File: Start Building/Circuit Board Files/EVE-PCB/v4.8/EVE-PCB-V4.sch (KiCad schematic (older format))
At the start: 50 parts, among them J1 PJ-102AH, J2 2x20 Male Header, J3 1725669, Q1 UA7805CKCT, Q12 DMN6140LQ-7, Q6 DMN6140LQ-7, Q7 DMN6140LQ-7, U1 PCA9685PW, U2 ADS1115IDGSR, U3 TLV4314IPWR, U4 TLV4314IPWR, U5 MCP1501-40E_SN

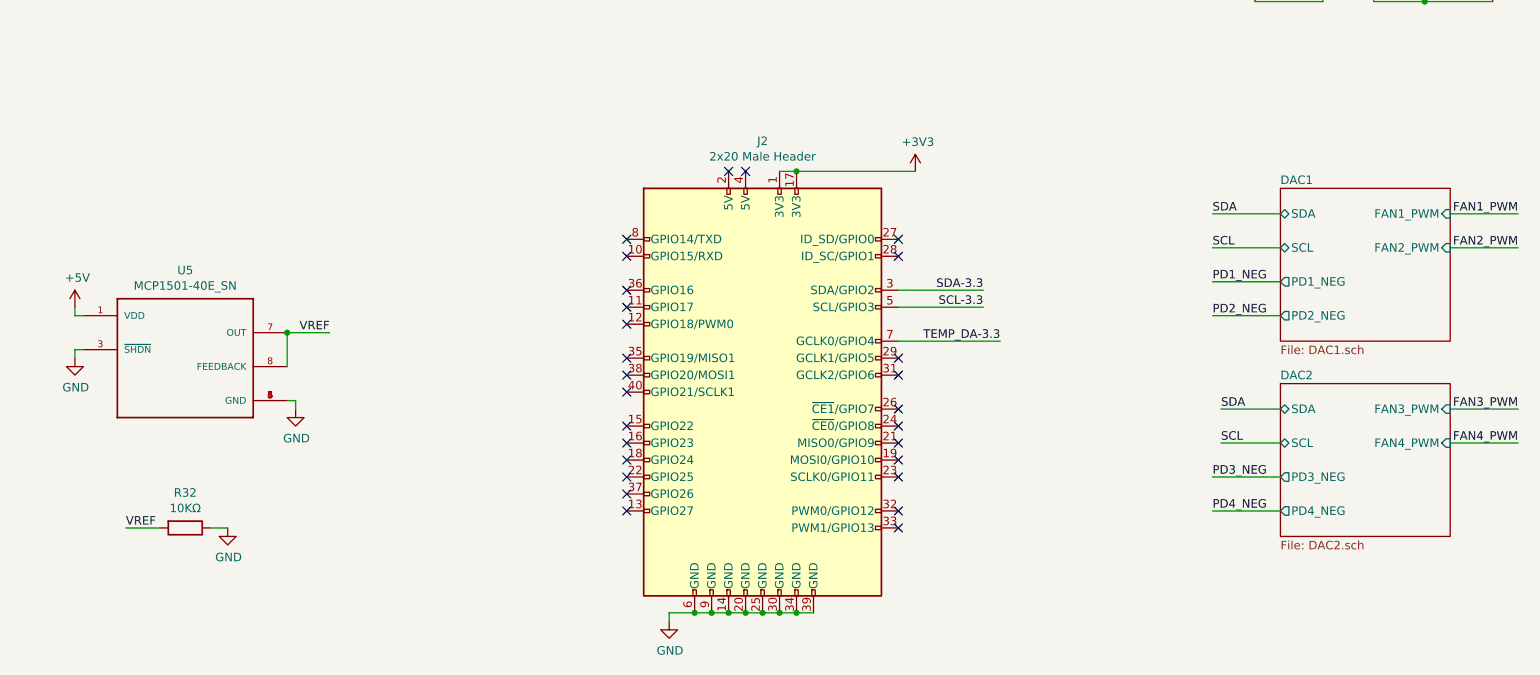
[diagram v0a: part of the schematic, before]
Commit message: Bump PCB version to 4.81
- Fixed voltages for fan and LED
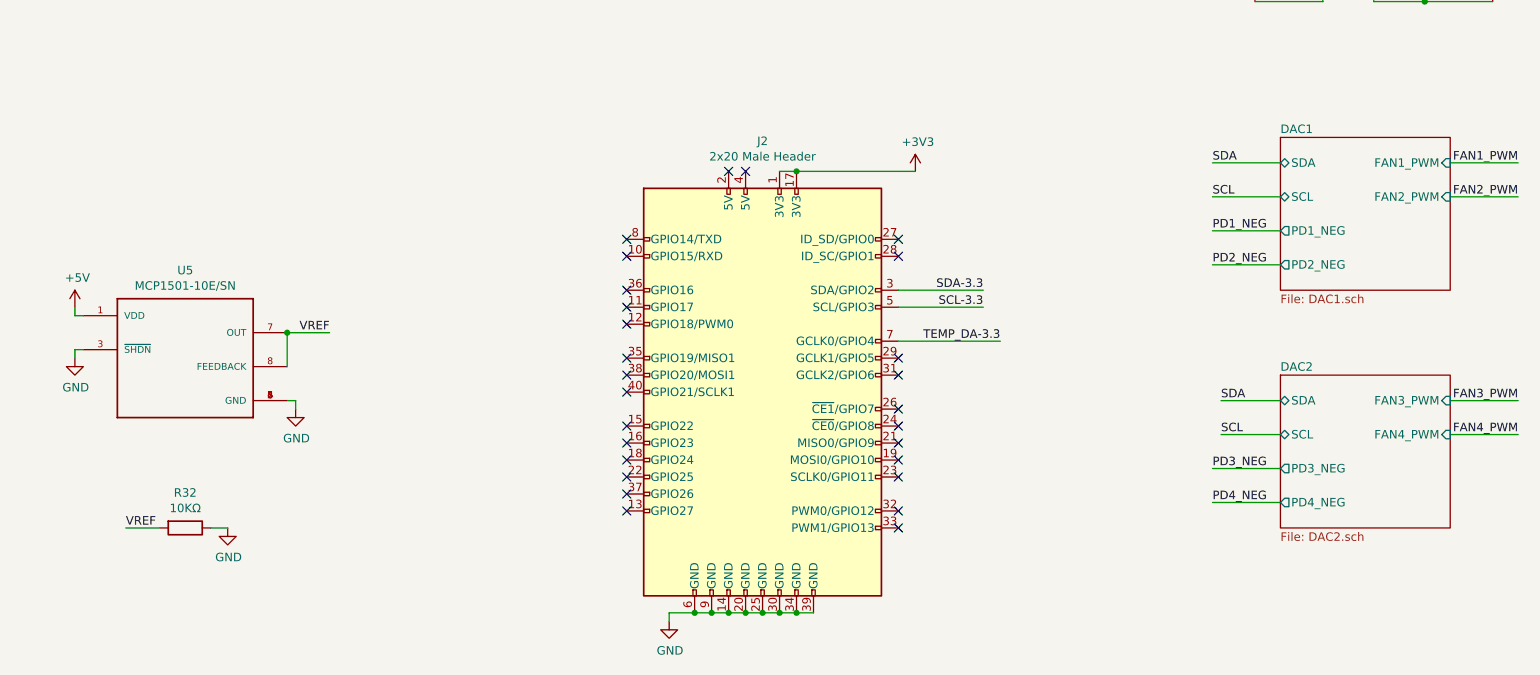
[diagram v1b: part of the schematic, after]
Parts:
- U5: value MCP1501-40E_SN -> MCP1501-10E/SN
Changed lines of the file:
@@
 P 7500 4600
 F 0 "U5" H 7500 5117 50  0000 C CNN
-F 1 "MCP1501-40E_SN" H 7500 5026 50  0000 C CNN
+F 1 "MCP1501-10E/SN" H 7500 5026 50  0000 C CNN
 F 2 "Package_SO:SOIC-8_3.9x4.9mm_P1.27mm" H 7500 4600 50  0001 L BNN
 F 3 "Microchip" H 7500 4600 50  0001 L BNN
@@
 $EndComp
 $Sheet
-S 13950 4750 1000 900
+S 13950 4700 1000 900
 U 5CA80A88
 F0 "DAC2" 50
 F1 "DAC2.sch" 50
-F2 "SDA" B L 13950 4900 50
-F3 "SCL" B L 13950 5100 50
-F4 "PD3_NEG" O L 13950 5300 50
-F5 "PD4_NEG" O L 13950 5500 50
-F6 "FAN3_PWM" I R 14950 4900 50
-F7 "FAN4_PWM" I R 14950 5100 50
+F2 "SDA" B L 13950 4850 50
+F3 "SCL" B L 13950 5050 50
+F4 "PD3_NEG" O L 13950 5250 50
+F5 "PD4_NEG" O L 13950 5450 50
+F6 "FAN3_PWM" I R 14950 4850 50
+F7 "FAN4_PWM" I R 14950 5050 50
 $EndSheet
 Wire Wire Line
-	15350 5100 14950 5100
-Wire Wire Line
-	15350 4900 14950 4900
-Text Label 15350 5100 2    50   ~ 0
+	15350 5050 14950 5050
+Wire Wire Line
+	15350 4850 14950 4850
+Text Label 15350 5050 2    50   ~ 0
 FAN4_PWM
-Text Label 15350 4900 2    50   ~ 0
+Text Label 15350 4850 2    50   ~ 0
 FAN3_PWM
 Wire Wire Line
-	15350 3950 14950 3950
-Wire Wire Line
-	15350 3750 14950 3750
-Text Label 15350 3950 2    50   ~ 0
+	15350 3650 14950 3650
+Wire Wire Line
+	15350 3450 14950 3450
+Text Label 15350 3650 2    50   ~ 0
 FAN2_PWM
-Text Label 15350 3750 2    50   ~ 0
+Text Label 15350 3450 2    50   ~ 0
 FAN1_PWM
 $Comp
@@
 $EndComp
 Wire Wire Line
-	13550 5500 13950 5500
-Wire Wire Line
-	13550 5300 13950 5300
-Text Label 13550 5500 0    50   ~ 0
+	13550 5450 13950 5450
+Wire Wire Line
+	13550 5250 13950 5250
+Text Label 13550 5450 0    50   ~ 0
 PD4_NEG
-Text Label 13550 5300 0    50   ~ 0
+Text Label 13550 5250 0    50   ~ 0
 PD3_NEG
 Wire Wire Line
-	13550 3950 13950 3950
-Wire Wire Line
-	13550 3750 13950 3750
-Text Label 13550 4150 0    50   ~ 0
+	13550 3650 13950 3650
+Wire Wire Line
+	13550 3450 13950 3450
+Text Label 13550 3850 0    50   ~ 0
 PD1_NEG
-Text Label 13550 4350 0    50   ~ 0
+Text Label 13550 4050 0    50   ~ 0
 PD2_NEG
 Wire Wire Line
-	13550 4150 13950 4150
-Wire Wire Line
-	13550 4350 13950 4350
+	13550 3850 13950 3850
+Wire Wire Line
+	13550 4050 13950 4050
 Connection ~ 14800 2100
 Wire Wire Line
@@
 	14800 1250 15300 1250
 Wire Wire Line
-	13600 5100 13950 5100
-Wire Wire Line
-	13600 4900 13950 4900
-Text Label 13600 5100 0    50   ~ 0
+	13600 5050 13950 5050
+Wire Wire Line
+	13600 4850 13950 4850
+Text Label 13600 5050 0    50   ~ 0
 SCL
-Text Label 13600 4900 0    50   ~ 0
+Text Label 13600 4850 0    50   ~ 0
 SDA
-Text Label 13550 3950 0    50   ~ 0
+Text Label 13550 3650 0    50   ~ 0
 SCL
-Text Label 13550 3750 0    50   ~ 0
+Text Label 13550 3450 0    50   ~ 0
 SDA
 $Sheet
-S 13950 3600 1000 900
+S 13950 3300 1000 900
 U 5CA7DFAE
 F0 "DAC1" 50
 F1 "DAC1.sch" 50
-F2 "SDA" B L 13950 3750 50
-F3 "SCL" B L 13950 3950 50
-F4 "PD1_NEG" O L 13950 4150 50
-F5 "PD2_NEG" O L 13950 4350 50
-F6 "FAN1_PWM" I R 14950 3750 50
-F7 "FAN2_PWM" I R 14950 3950 50
+F2 "SDA" B L 13950 3450 50
+F3 "SCL" B L 13950 3650 50
+F4 "PD1_NEG" O L 13950 3850 50
+F5 "PD2_NEG" O L 13950 4050 50
+F6 "FAN1_PWM" I R 14950 3450 50
+F7 "FAN2_PWM" I R 14950 3650 50
 $EndSheet
 Wire Wire Line

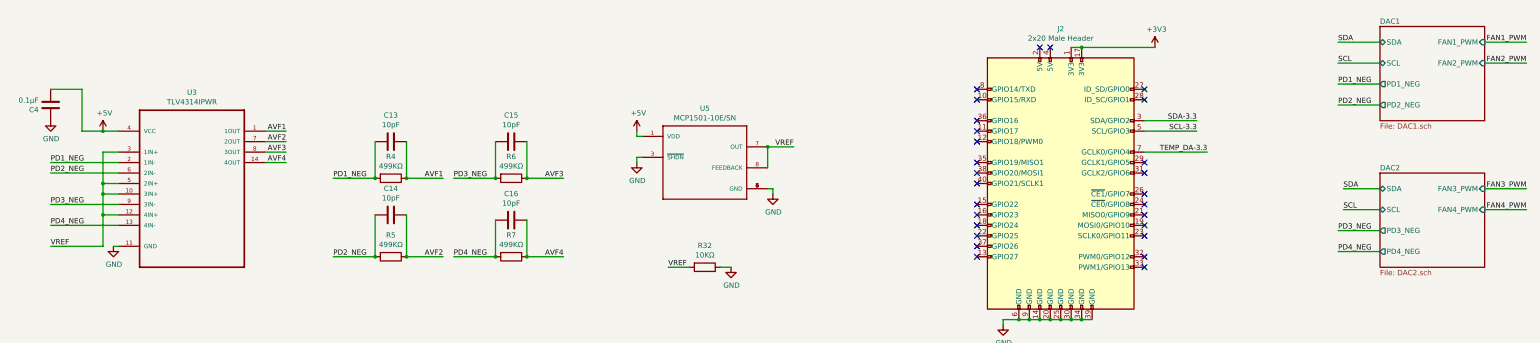
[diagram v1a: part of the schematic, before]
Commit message: Bump PCB to version 4.82
- Update schematic to use V_ref as PD positive terminal.
- Update PCB to allow for this change.
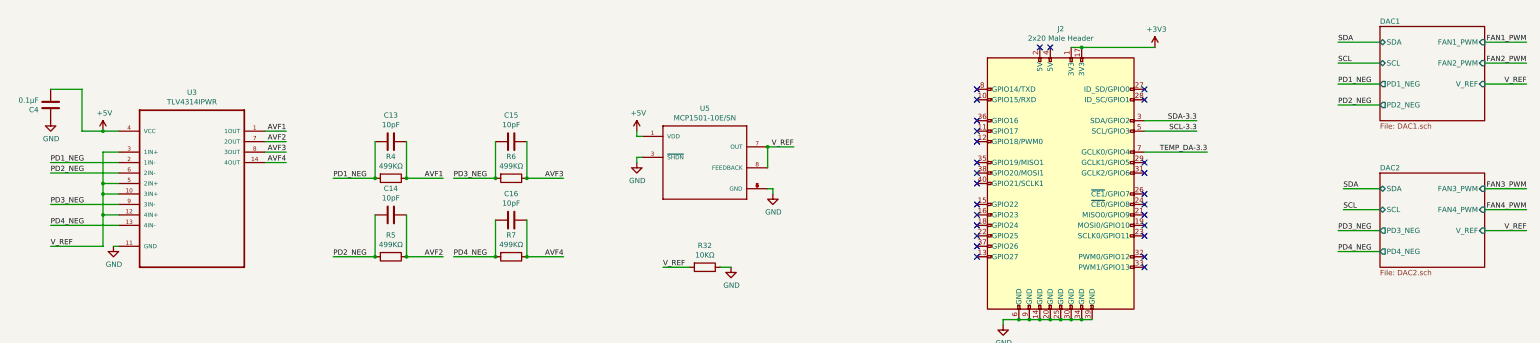
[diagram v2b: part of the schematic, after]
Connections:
- net VREF renamed V_REF
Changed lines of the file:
@@
 Connection ~ 1750 5100
 Text Label 1250 5400 0    50   ~ 0
-VREF
+V_REF
 Wire Wire Line
 	1750 5400 1250 5400
 Wire Wire Line
 	1750 5100 1750 5400
-Text Label 7150 5600 0    50   ~ 0
-VREF
-Wire Wire Line
-	7150 5600 7350 5600
 $Comp
 L EVE-PCB-V4-rescue:GND-power-EVE-PCB-rescue #PWR01
@@
 $EndComp
 Text Label 8350 4450 2    50   ~ 0
-VREF
+V_REF
 $Comp
 L MCP1501-40E_SN:MCP1501-40E_SN U5
@@
 F6 "FAN3_PWM" I R 14950 4850 50
 F7 "FAN4_PWM" I R 14950 5050 50
+F8 "V_REF" I R 14950 5250 50
 $EndSheet
 Wire Wire Line
@@
 F6 "FAN1_PWM" I R 14950 3450 50
 F7 "FAN2_PWM" I R 14950 3650 50
+F8 "V_REF" I R 14950 3850 50
 $EndSheet
 Wire Wire Line
@@
 SCL-3.3
 Connection ~ 13000 7600
+Text Label 15350 3850 2    50   ~ 0
+V_REF
+Wire Wire Line
+	15350 3850 14950 3850
+Text Label 15350 5250 2    50   ~ 0
+V_REF
+Wire Wire Line
+	15350 5250 14950 5250
+Text Label 7100 5600 0    50   ~ 0
+V_REF
+Wire Wire Line
+	7100 5600 7350 5600
 $EndSCHEMATC
